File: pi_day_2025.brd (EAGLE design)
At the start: 70 x 79.5 mm, 109 parts, among them IC1 W25Q64JVXGIQ, J4 SM03B-SRSS-TB(LF)(SN), Q2 310mA/60V/1.6Ω, U1 APS6404L-3SQR-ZR, U2 RP2350A, U3 TPS76318DBVRG4, U4 TPS63001DRCR, U5 TXS0108EPWRG4, U6 LSM6DS3TR-C, U7 MCP73833T-AMI/MF, U8 TPS2113APWR, U9 ESP32-C3-MINI-1-N4, Y1 12MHz

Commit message: Update pi_day_2025.brd
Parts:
- moved U9 62.6 mm to (-24.6, 19.6), turned to 50 degrees
- moved S1 41.6 mm to (11.5, -39.3)
- moved C1 37.3 mm to (7.80, -28.7), turned to 270 degrees
- moved R13 35.3 mm to (-1.07, -20.3), turned to 90 degrees
- moved R12 34.2 mm to (-0.13, -20.3), turned to 90 degrees
- moved R15 32.4 mm to (-1.14, -4.19)
- moved U1 32.0 mm to (9.07, -26.2), turned to 180 degrees
- moved Y1 30.9 mm to (1.09, -3.63)
- moved R1 30.3 mm to (10.4, -29.0), turned to 90 degrees
- moved IC1 29.4 mm to (9.32, -22.1), turned to 180 degrees
- moved R2 20.5 mm to (7.95, -10.7), turned to 0 degrees
- moved D9 9.30 mm to (18.0, -25.4)
- moved U2 3.34 mm to (0.28, -12.3)

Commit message: Placed components
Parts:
- moved C48 336.9 mm to (30.1, -10.7), turned to 180 degrees
- moved C47 333.9 mm to (30.1, -12.0), turned to 180 degrees
- moved R23 329.0 mm to (15.5, -13.8), turned to 90 degrees
- moved C15 230.1 mm to (-21.9, -14.5), turned to 90 degrees
- moved C25 222.3 mm to (-108.2, -66.1)
- moved C26 222.3 mm to (-108.2, -69.2)
- moved C45 222.3 mm to (-108.2, -79.1)
- moved C16 222.3 mm to (-108.2, -21.7)
- moved C19 222.3 mm to (-88.9, 14.1)
- moved C21 222.3 mm to (-108.2, -43.3)
- moved C22 222.3 mm to (-108.2, -46.3)
- moved C23 222.3 mm to (-108.2, -57.0)
- moved C24 222.3 mm to (-108.2, -63.1)
- moved C44 222.3 mm to (-108.2, -75.8)
- moved D13 222.3 mm to (-99.6, -11.8)
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
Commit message: Update pi_day_2025.brd
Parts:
- moved C46 144.8 mm to (14.3, -5.18), turned to 180 degrees
- moved U5 106.0 mm to (16.5, -0.81), turned to 180 degrees
- moved MK1 101.3 mm to (24.4, -3.15), turned to 180 degrees
- moved U6 76.6 mm to (-11.4, 21.4), turned to 270 degrees
- moved C34 43.0 mm to (-6.68, -18.4), turned to 180 degrees
- moved C32 42.6 mm to (-6.68, -17.4), turned to 180 degrees
- moved R7 42.2 mm to (-7.39, 20.7), turned to 0 degrees
- moved R6 42.2 mm to (-7.39, 22.1), turned to 0 degrees
- moved C29 39.9 mm to (5.61, -18.6), turned to 0 degrees
- moved C36 39.8 mm to (-2.57, -23.4), turned to 180 degrees
- moved C37 39.3 mm to (-2.41, -21.7), turned to 270 degrees
- moved C38 37.4 mm to (6.83, -16.6), turned to 0 degrees
- moved C18 36.2 mm to (-10.0, -19.4)
- moved C30 36.1 mm to (6.83, -15.2), turned to 0 degrees
- moved C39 35.7 mm to (-3.15, -8.56)
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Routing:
- net 3.3V: track 0.66 -> 0.00 mm

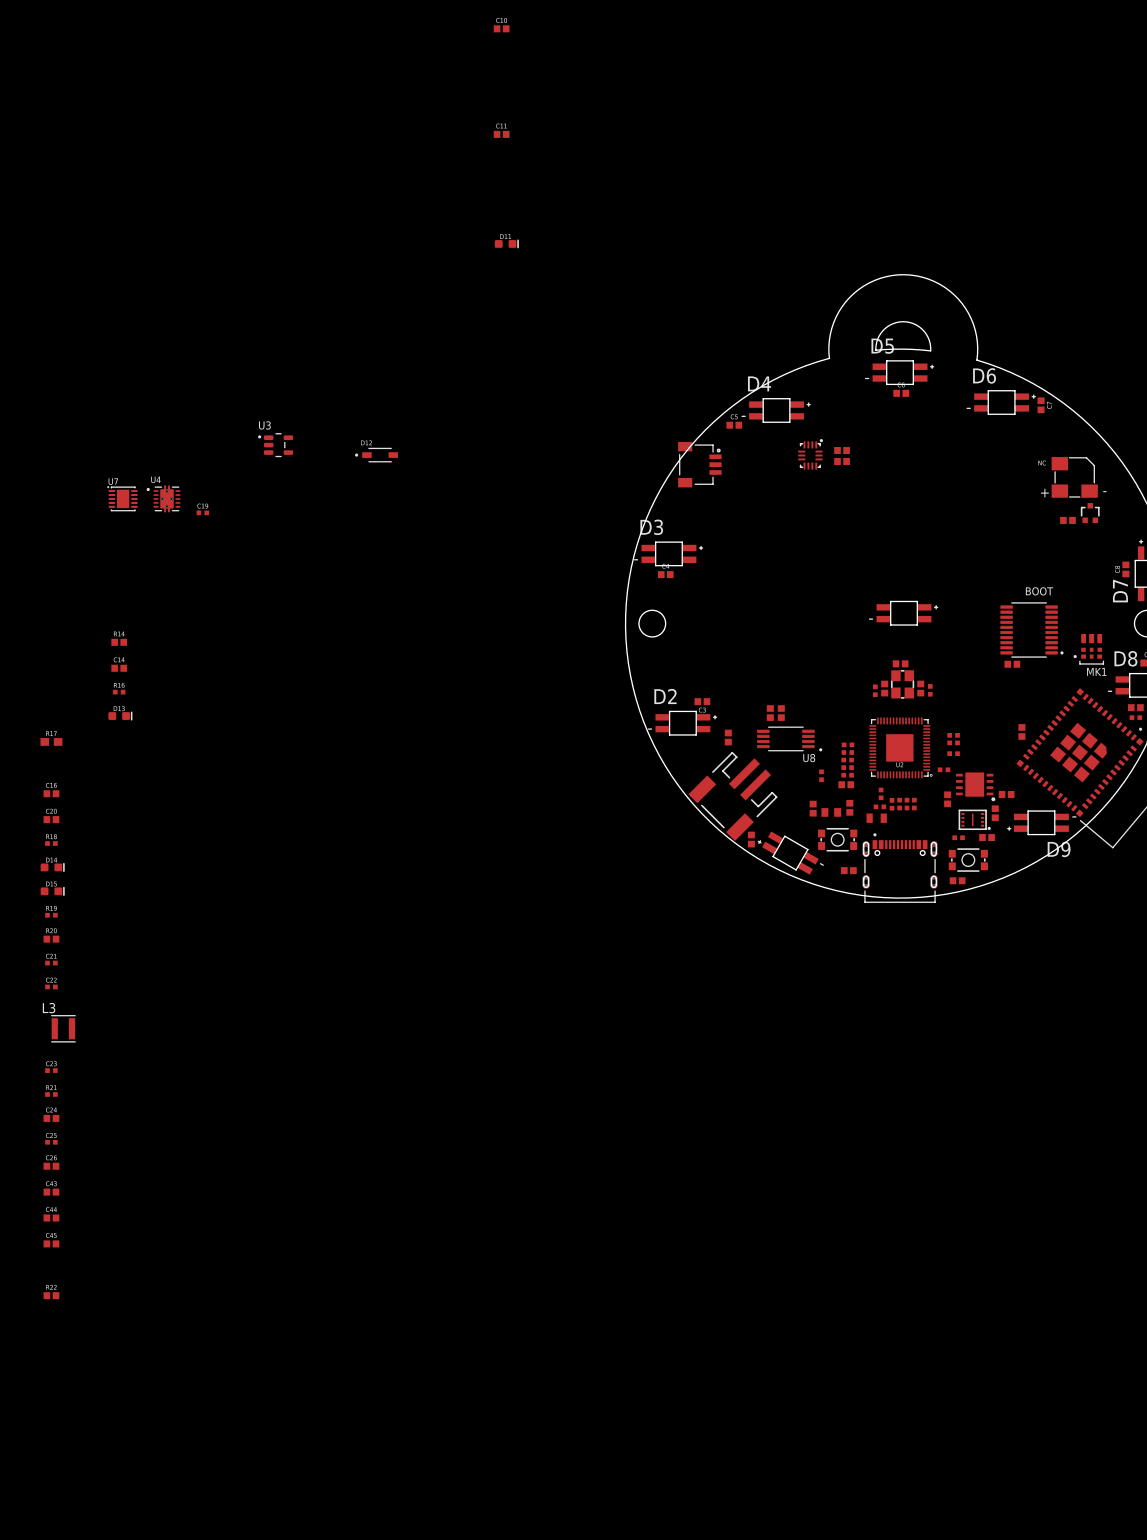
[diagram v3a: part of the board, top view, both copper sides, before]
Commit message: Added voltage symbols
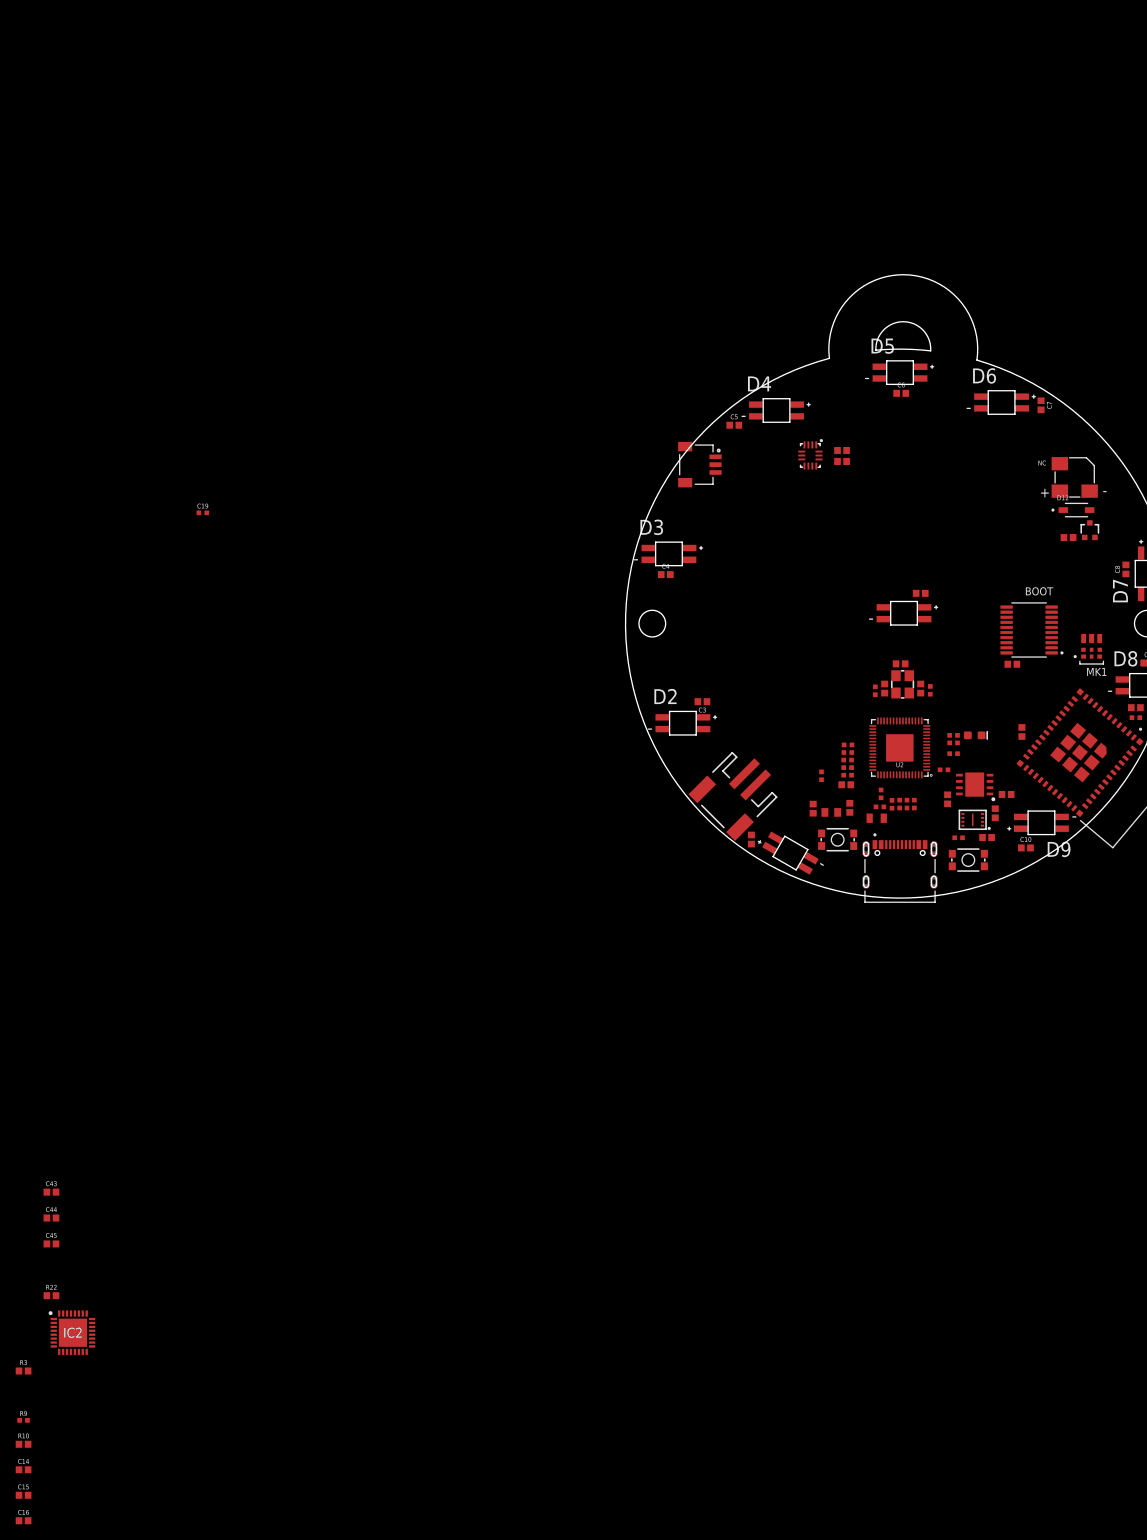
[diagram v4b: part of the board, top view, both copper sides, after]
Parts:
- removed C20, C26: 1.0uF, SparkFun-Capacitors:0402
- removed C21, C22, C23: 10uF, SparkFun-Capacitors:0402-TIGHT
- removed C24: 0.1uF, SparkFun-Capacitors:0402
- removed C25: 4.7uF, SparkFun-Capacitors:0402-TIGHT
- removed D13, D14, D15: GREEN, SparkFun-LED:LED-0603
- removed L3: LQH3NPN2R2MJRL, LQH3NPN2R2MJRL:IND_LQH3NPN2R2MJRL
- removed R14: 499, SparkFun-Resistors:0402@1
- removed R16, R18, R19: 220, SparkFun-Resistors:0402-TIGHT
- removed R17: 10k, SparkFun-Resistors:0603
- removed R20: 1K, SparkFun-Resistors:0402@1
- removed R21: 100, SparkFun-Resistors:0402-TIGHT
- removed R8: 5.1K, SparkFun-Resistors:0402@1
- removed U3: TPS76318DBVRG4, TPS76318DBVRG4:SOT95P280X145-5N
- removed U4: TPS63001DRCR, TPS63001DRCR:VREG_V62/16624-01YE
- removed U7: MCP73833T-AMI/MF, MCP73833T-AMI_MF:SON50P300X300X100-11N
- removed U8: TPS2113APWR, TPS2113APWR:SOP65P640X120-8N
- added IC2: NPM1300-QEAA-R, SamacSys_Parts:QFN50P500X500X90-33N
- C14, C15: value 0.1uF -> 1.0uF
- C16: value 1.0uF -> 0.1uF
- R10: value 100K -> 470K; device SparkFun-Resistors:0402@1 -> SparkFun-Resistors:0402
- R11, R15, R22: device SparkFun-Resistors:0402@1 -> SparkFun-Resistors:0402
- R3: value 5.1K -> 10k; device SparkFun-Resistors:0402@1 -> SparkFun-Resistors:0402
- R4: value DNF -> (none); device SparkFun-Resistors:0402@1 -> SparkFun-Resistors:0402
- R5: value 1K -> (none); device SparkFun-Resistors:0402@1 -> SparkFun-Resistors:0402
- R6, R7: value 2.2K -> (none); device SparkFun-Resistors:0402@1 -> SparkFun-Resistors:0402
- R9: value 100K -> 47k; device SparkFun-Resistors:0402@1 -> SparkFun-Resistors:0402-TIGHT
- moved R10 133.3 mm to (-111.8, -104.6), turned to 0 degrees
- moved R9 132.2 mm to (-111.8, -101.6), turned to 0 degrees
- moved C15 132.0 mm to (-111.8, -111.2), turned to 0 degrees
- moved C10 124.0 mm to (16.1, -28.6)
- moved R3 123.1 mm to (-111.8, -95.3)
- moved C14 102.9 mm to (-111.8, -107.9)
- moved C16 92.8 mm to (-111.8, -114.4)
- moved D12 89.1 mm to (22.5, 14.5)
- moved D11 86.6 mm to (9.53, -14.2)
- moved C11 79.3 mm to (2.64, 3.86), turned to 180 degrees
- moved R25 2.19 mm to (21.5, 11.0)
- moved Q2 2.18 mm to (24.2, 11.9)
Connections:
- removed net N$10: D13.C, U8.1
- removed net N$14: R17.2, U7.8
- removed net N$15: D14.A, R18.1
- removed net N$16: D14.C, U7.7
- removed net N$17: D15.A, R19.1
- removed net N$18: D15.C, U7.4
- removed net N$19: R20.2, U7.6
- removed net N$20: L3.2, U4.4
- removed net N$21: L3.1, U4.2
- removed net N$22: C24.1, R21.1, U4.6, U4.7, U4.8
- removed net N$8: R14.2, U8.4
- removed net N$9: D13.A, R16.1
- removed net VIN: C23.1, R21.2, U4.5, U8.7
- removed net V_BATT: C15.1, C20.1, J1.2, U7.10, U7.9, U8.6
- new net LSIN1/VINLDO1: IC2.28
- new net LSIN2/VINLDO2: IC2.30
- new net LSOUT1/VOUTLDO1: IC2.29
- new net LSOUT2/VOUTLDO2: IC2.31
- new net N$38: J1.2
- new net PVDD: IC2.4
- new net PVSS1: IC2.2
- new net PVSS2: IC2.6
- new net SW1: IC2.3
- new net SW2: IC2.5
- new net USB_CC1: IC2.23
- new net USB_CC2: CONN1.B5, IC2.24
- new net VBAT: IC2.19
- new net VOUT1: IC2.1
- new net VOUT2: IC2.32
- new net VSYS: IC2.20
- net 1.8V: no longer C25.1, U3.5
- net 3.3V: now also C16.2, IC2.12; no longer C21.1, C22.1, C26.1, U3.1, U3.3, U4.1, U4.10
- net CHARGE_STAT: no longer U7.3
- net GND: now also C14.2, IC2.33, R10.1, R3.2, R9.1; no longer C14.1, C20.2, C21.2, C22.2, C23.2, C24.2, C25.2, C26.2, R10.2, R14.1, R17.1, R20.1, R3.1, R8.1, U3.2, U4.11, U4.12, U4.13, U4.14, U4.15, U4.3, U4.9, U7.11, U7.5, U8.2, U8.5
- net N$3: now also IC2.18, R3.1; no longer CONN1.A5, R3.2
- net N$6: now also IC2.16, R10.2; no longer R10.1, R9.2, U8.3
- net N$7: now also IC2.17, R9.2; no longer CONN1.B5, R8.2
- net SCL: now also IC2.14
- net SDA: now also IC2.13
- net V_USB: now also C14.1, C15.1, IC2.21, IC2.22; no longer C14.2, C16.2, R16.2, R18.2, R19.2, R9.1, U7.1, U7.2, U8.8

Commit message: more modification
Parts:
- added R8: 0, SparkFun-Resistors:0603
- R10: value 470K -> (none)
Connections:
- new net N$8: IC2.15, R8.2
- net GND: now also R8.1
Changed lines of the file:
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@@
 <attribute name="VALUE" x="-111.76" y="-102.162" size="0.6096" layer="27" font="vector" ratio="20" align="top-center"/>
 </element>
-<element name="R10" library="SparkFun-Resistors" library_urn="urn:adsk.eagle:library:532" package="0402" package3d_urn="urn:adsk.eagle:package:39657/2" value="470K" x="-111.76" y="-104.648" smashed="yes">
+<element name="R10" library="SparkFun-Resistors" library_urn="urn:adsk.eagle:library:532" package="0402" package3d_urn="urn:adsk.eagle:package:39657/2" value=" " x="-111.76" y="-104.648" smashed="yes">
 <attribute name="NAME" x="-111.76" y="-103.886" size="0.6096" layer="25" font="vector" ratio="20" align="bottom-center"/>
 <attribute name="PROD_ID" value=" " x="-111.76" y="-104.648" size="1.778" layer="27" display="off"/>
@@
 <attribute name="PROD_ID" value="CAP-12416" x="-111.76" y="-114.4016" size="1.778" layer="27" display="off"/>
 <attribute name="VALUE" x="-111.76" y="-115.1636" size="0.6096" layer="27" font="vector" ratio="20" align="top-center"/>
+</element>
+<element name="R8" library="SparkFun-Resistors" library_urn="urn:adsk.eagle:library:532" package="0603" package3d_urn="urn:adsk.eagle:package:41389018/1" value="0" x="-111.76" y="-117.6528" smashed="yes">
+<attribute name="NAME" x="-111.76" y="-116.8908" size="0.6096" layer="25" font="vector" ratio="20" align="bottom-center"/>
+<attribute name="PROD_ID" value="RES-08609" x="-111.76" y="-117.6528" size="1.778" layer="27" display="off"/>
+<attribute name="VALUE" x="-111.76" y="-118.4148" size="0.6096" layer="27" font="vector" ratio="20" align="top-center"/>
 </element>
 </elements>
@@
 <contactref element="C15" pad="2"/>
 <contactref element="C16" pad="1"/>
+<contactref element="R8" pad="1"/>
+<wire x1="-112.34" y1="-114.4016" x2="-112.61" y2="-117.6528" width="0" layer="19" extent="1-1"/>
 <wire x1="-111.18" y1="-111.1504" x2="-112.34" y2="-114.4016" width="0" layer="19" extent="1-1"/>
 <wire x1="-111.18" y1="-107.8992" x2="-111.18" y2="-111.1504" width="0" layer="19" extent="1-1"/>
@@
 <wire x1="-103.0108" y1="-92.174" x2="-111.26" y2="-101.6" width="0" layer="19" extent="1-1"/>
 </signal>
+<signal name="N$8">
+<contactref element="R8" pad="2"/>
+<contactref element="IC2" pad="15"/>
+<wire x1="-104.2108" y1="-92.874" x2="-110.91" y2="-117.6528" width="0" layer="19" extent="1-1"/>
+</signal>
 </signals>

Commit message: update
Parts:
- added S3: JS202011JCQN, JS202011JCQN:SW_JS202011JCQN
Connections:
- removed net VBAT: IC2.19
- new net N$9: S3.7
- new net V_BATT: IC2.19, S3.6
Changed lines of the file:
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@@
 <attribute name="VALUE" x="-111.76" y="-118.4148" size="0.6096" layer="27" font="vector" ratio="20" align="top-center"/>
+</element>
+<element name="S3" library="JS202011JCQN" package="SW_JS202011JCQN" value="JS202011JCQN" x="-118.6688" y="-112.3696" smashed="yes">
+<attribute name="AVAILABILITY" value="In Stock" x="-118.6688" y="-112.3696" size="1.778" layer="27" display="off"/>
+<attribute name="CHECK_PRICES" value="https://www.snapeda.com/parts/JS202011JCQN/C%2526K/view-part/?ref=eda" x="-118.6688" y="-112.3696" size="1.778" layer="27" display="off"/>
+<attribute name="DESCRIPTION" value=" Slide Switch DPDT Surface Mount " x="-118.6688" y="-112.3696" size="1.778" layer="27" display="off"/>
+<attribute name="MF" value="C&amp;K" x="-118.6688" y="-112.3696" size="1.778" layer="27" display="off"/>
+<attribute name="MP" value="JS202011JCQN" x="-118.6688" y="-112.3696" size="1.778" layer="27" display="off"/>
+<attribute name="NAME" x="-121.1688" y="-107.3696" size="1.27" layer="25"/>
+<attribute name="PACKAGE" value="DPDT-6 C&amp;amp;K" x="-118.6688" y="-112.3696" size="1.778" layer="27" display="off"/>
+<attribute name="PRICE" value="None" x="-118.6688" y="-112.3696" size="1.778" layer="27" display="off"/>
+<attribute name="SNAPEDA_LINK" value="https://www.snapeda.com/parts/JS202011JCQN/C%2526K/view-part/?ref=snap" x="-118.6688" y="-112.3696" size="1.778" layer="27" display="off"/>
+<attribute name="VALUE" x="-121.1688" y="-117.3696" size="1.27" layer="27" align="top-left"/>
 </element>
 </elements>
@@
 <contactref element="IC2" pad="20"/>
 </signal>
-<signal name="VBAT">
-<contactref element="IC2" pad="19"/>
-</signal>
 <signal name="VOUT2">
 <contactref element="IC2" pad="32"/>
@@
 <wire x1="-104.2108" y1="-92.874" x2="-110.91" y2="-117.6528" width="0" layer="19" extent="1-1"/>
 </signal>
+<signal name="N$9">
+<contactref element="S3" pad="7"/>
+</signal>
+<signal name="V_BATT">
+<contactref element="S3" pad="6"/>
+<contactref element="IC2" pad="19"/>
+<wire x1="-103.0108" y1="-91.174" x2="-117.4688" y2="-112.3696" width="0" layer="19" extent="1-1"/>
+</signal>
 </signals>

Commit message: Checking in
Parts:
- added C20: 2.2UF, SparkFun-Capacitors_Sai:0402
- added C21, C22, C23, C24: 10uF, SparkFun-Capacitors_Sai:0402
- added L3, L4: 2.2uH, LQM2MPN4R7MG0L:INDC2016X100N
- added LED1: EAST1616RGYA0, EAST1616RGYA0:EAST1616RGYA0
- added R14, R16: 0, SparkFun-Resistors_Sai:0402
- R8: device SparkFun-Resistors:0603 -> SparkFun-Resistors_Sai:0402
- R9: value 47k -> 47KOHM-0402-1/10W-10%; device SparkFun-Resistors:0402-TIGHT -> SparkFun-Resistors_Sai:0402
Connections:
- removed net PVDD: IC2.4
- removed net SW1: IC2.3
- removed net SW2: IC2.5
- removed net VOUT1: IC2.1
- removed net VOUT2: IC2.32
- new net !INT_NPM1300: IC2.8, U2.10
- new net LED0: IC2.25, LED1.3
- new net LED1: IC2.26, LED1.4
- new net LED2: IC2.27, LED1.1
- new net N$10: IC2.3, L3.1
- new net N$14: IC2.5, L4.1
- net 1.8V: now also C24.1, IC2.1, L3.2
- net 3.3V: now also IC2.32, L4.2
- net GND: now also C20.2, C21.2, R14.1, R16.1
- net PVSS1: now also C23.2, C24.2, R16.2
- net PVSS2: now also C22.2, R14.2
- net VSYS: now also C21.1, C22.1, C23.1, IC2.4, LED1.2
- net V_BATT: now also C20.1
